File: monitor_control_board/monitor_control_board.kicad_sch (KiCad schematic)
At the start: 21 parts, among them J2 Conn_01x08_Male, J3 Conn_01x08_Male, J5 Conn_01x05_Male, J6 Conn_01x05_Male, SW1 SW_Push, SW2 SW_Push, SW3 SW_Push, SW4 SW_Push, SW5 SW_Push, SW6 SW_Push, U1 TSSP58038

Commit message: osd 컨트롤 보드 좌표 미세 보정
Signed-off-by: Ju, Gyeong-min <jcmh74@gmail.com>
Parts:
- SW1, SW2, SW3, SW4, SW5: footprint Button_Switch_THT:SW_PUSH-12mm -> monitor_control_board_library:SW_PUSH-12mm_Complex
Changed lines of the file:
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@@
     )
     (property "Value" "SW_Push" (id 1) (at 226.695 73.914 0))
-    (property "Footprint" "Button_Switch_THT:SW_PUSH-12mm" (id 2) (at 226.695 67.31 0)
+    (property "Footprint" "monitor_control_board_library:SW_PUSH-12mm_Complex" (id 2) (at 226.695 67.31 0)
       (effects (font (size 1.27 1.27)) hide)
     )
@@
     )
     (property "Value" "SW_Push" (id 1) (at 204.47 73.914 0))
-    (property "Footprint" "Button_Switch_THT:SW_PUSH-12mm" (id 2) (at 204.47 67.31 0)
+    (property "Footprint" "monitor_control_board_library:SW_PUSH-12mm_Complex" (id 2) (at 204.47 67.31 0)
       (effects (font (size 1.27 1.27)) hide)
     )
@@
     )
     (property "Value" "SW_Push" (id 1) (at 203.835 51.054 0))
-    (property "Footprint" "Button_Switch_THT:SW_PUSH-12mm" (id 2) (at 203.835 44.45 0)
+    (property "Footprint" "monitor_control_board_library:SW_PUSH-12mm_Complex" (id 2) (at 203.835 44.45 0)
       (effects (font (size 1.27 1.27)) hide)
     )
@@
   (symbol (lib_id "power:PWR_FLAG") (at 81.28 53.34 270) (unit 1)
     (in_bom yes) (on_board yes) (fields_autoplaced)
-    (property "Reference" "#FLG?" (id 0) (at 83.185 53.34 0)
+    (property "Reference" "#FLG0101" (id 0) (at 83.185 53.34 0)
       (effects (font (size 1.27 1.27)) hide)
     )
@@
     )
     (property "Value" "SW_Push" (id 1) (at 204.47 97.409 0))
-    (property "Footprint" "Button_Switch_THT:SW_PUSH-12mm" (id 2) (at 204.47 90.805 0)
+    (property "Footprint" "monitor_control_board_library:SW_PUSH-12mm_Complex" (id 2) (at 204.47 90.805 0)
       (effects (font (size 1.27 1.27)) hide)
     )
@@
     )
     (property "Value" "SW_Push" (id 1) (at 181.61 74.549 0))
-    (property "Footprint" "Button_Switch_THT:SW_PUSH-12mm" (id 2) (at 181.61 67.945 0)
+    (property "Footprint" "monitor_control_board_library:SW_PUSH-12mm_Complex" (id 2) (at 181.61 67.945 0)
       (effects (font (size 1.27 1.27)) hide)
     )
@@
   (symbol_instances
     (path "/94b5e945-5454-483f-a874-b3e91dafa008"
-      (reference "#FLG?") (unit 1) (value "PWR_FLAG") (footprint "")
+      (reference "#FLG0101") (unit 1) (value "PWR_FLAG") (footprint "")
     )
     (path "/bc319651-4db4-432c-99a9-47f722955312"
@@
     )
     (path "/d0754a39-0cf1-4bbe-83a4-6155f2cbc878"
-      (reference "SW1") (unit 1) (value "SW_Push") (footprint "Button_Switch_THT:SW_PUSH-12mm")
+      (reference "SW1") (unit 1) (value "SW_Push") (footprint "monitor_control_board_library:SW_PUSH-12mm_Complex")
     )
     (path "/4d2bcc63-a2dd-418c-bd5f-ddaef4fca43f"
-      (reference "SW2") (unit 1) (value "SW_Push") (footprint "Button_Switch_THT:SW_PUSH-12mm")
+      (reference "SW2") (unit 1) (value "SW_Push") (footprint "monitor_control_board_library:SW_PUSH-12mm_Complex")
     )
     (path "/19cf3f75-846d-40c4-99e9-986cfa896c10"
-      (reference "SW3") (unit 1) (value "SW_Push") (footprint "Button_Switch_THT:SW_PUSH-12mm")
+      (reference "SW3") (unit 1) (value "SW_Push") (footprint "monitor_control_board_library:SW_PUSH-12mm_Complex")
     )
     (path "/98e08b96-ee1b-4bfe-acf7-0dc72d6a3691"
-      (reference "SW4") (unit 1) (value "SW_Push") (footprint "Button_Switch_THT:SW_PUSH-12mm")
+      (reference "SW4") (unit 1) (value "SW_Push") (footprint "monitor_control_board_library:SW_PUSH-12mm_Complex")
     )
     (path "/1436a783-6564-4cf1-b04a-2e5a11e5eb64"
-      (reference "SW5") (unit 1) (value "SW_Push") (footprint "Button_Switch_THT:SW_PUSH-12mm")
+      (reference "SW5") (unit 1) (value "SW_Push") (footprint "monitor_control_board_library:SW_PUSH-12mm_Complex")
     )
     (path "/06fc7b9c-8a77-4564-ae4b-423182fb3d64"

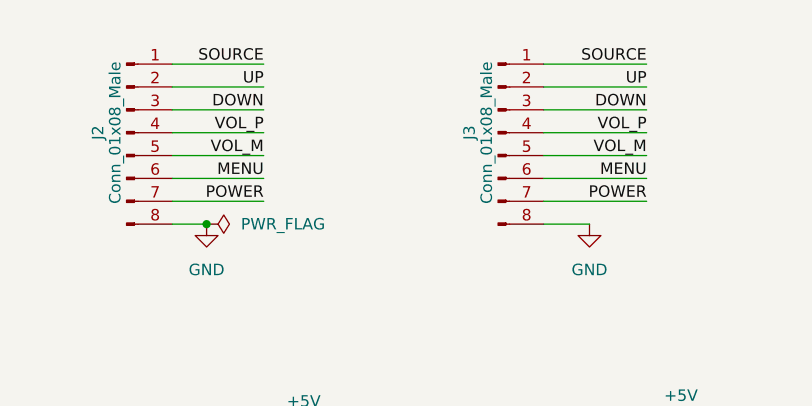
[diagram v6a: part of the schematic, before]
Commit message: osd 컨트롤 보드 GND 핀 추가
Signed-off-by: Ju, Gyeong-min <jcmh74@gmail.com>
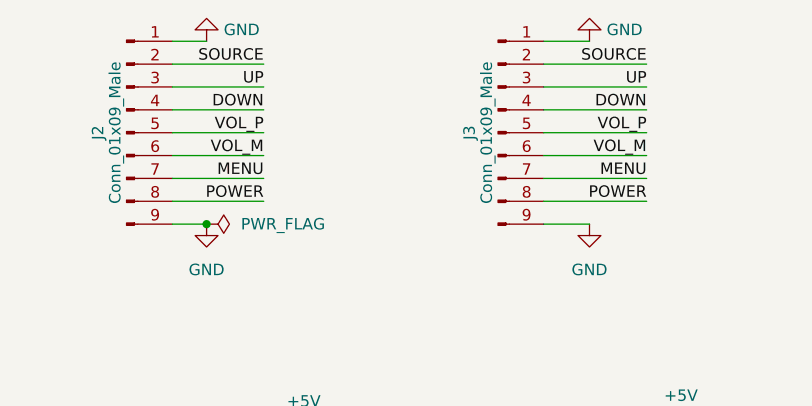
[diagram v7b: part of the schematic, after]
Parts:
- J2: value Conn_01x08_Male -> Conn_01x09_Male; footprint Connector_PinHeader_2.54mm:PinHeader_1x08_P2.54mm_Vertical -> Connector_PinHeader_2.54mm:PinHeader_1x09_P2.54mm_Vertical; symbol Connector:Conn_01x08_Male -> Connector:Conn_01x09_Male
- J3: value Conn_01x08_Male -> Conn_01x09_Male; footprint Connector_JST:JST_PH_S8B-PH-K_1x08_P2.00mm_Horizontal -> Connector_JST:JST_PH_S9B-PH-K_1x09_P2.00mm_Horizontal; symbol Connector:Conn_01x08_Male -> Connector:Conn_01x09_Male
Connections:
- net DOWN: now also J2.4 (Pin_4), J3.4 (Pin_4); no longer J2.3 (Pin_3), J3.3 (Pin_3)
- net GND: now also J2.1 (Pin_1), J2.9 (Pin_9), J3.1 (Pin_1), J3.9 (Pin_9); no longer J2.8 (Pin_8), J3.8 (Pin_8)
- net MENU: now also J2.7 (Pin_7), J3.7 (Pin_7); no longer J2.6 (Pin_6), J3.6 (Pin_6)
- net POWER: now also J2.8 (Pin_8), J3.8 (Pin_8); no longer J2.7 (Pin_7), J3.7 (Pin_7)
- net SOURCE: now also J2.2 (Pin_2), J3.2 (Pin_2); no longer J2.1 (Pin_1), J3.1 (Pin_1)
- net UP: now also J2.3 (Pin_3), J3.3 (Pin_3); no longer J2.2 (Pin_2), J3.2 (Pin_2)
- net VOL_M: now also J2.6 (Pin_6), J3.6 (Pin_6); no longer J2.5 (Pin_5), J3.5 (Pin_5)
- net VOL_P: now also J2.5 (Pin_5), J3.5 (Pin_5); no longer J2.4 (Pin_4), J3.4 (Pin_4)
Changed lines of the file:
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@@
+    (stroke (width 0) (type default) (color 0 0 0 0))
+  )
+  (wire (pts (xy 123.825 33.02) (xy 118.745 33.02))
     (stroke (width 0) (type default) (color 0 0 0 0))
   )
@@
   )
   (wire (pts (xy 87.63 40.64) (xy 77.47 40.64))
+    (stroke (width 0) (type default) (color 0 0 0 0))
+  )
+  (wire (pts (xy 77.47 33.02) (xy 81.28 33.02))
     (stroke (width 0) (type default) (color 0 0 0 0))
   )
@@
     (pin "2")
   )
+  (symbol (lib_id "power:GND") (at 123.825 33.02 180) (unit 1)
+    (in_bom yes) (on_board yes) (fields_autoplaced)
+    (property "Reference" "#PWR0109" (id 0) (at 123.825 26.67 0)
+      (effects (font (size 1.27 1.27)) hide)
+    )
+    (property "Value" "GND" (id 1) (at 125.73 31.7499 0)
+      (effects (font (size 1.27 1.27)) (justify right))
+    )
+    (property "Footprint" "" (id 2) (at 123.825 33.02 0)
+      (effects (font (size 1.27 1.27)) hide)
+    )
+    (property "Datasheet" "" (id 3) (at 123.825 33.02 0)
+      (effects (font (size 1.27 1.27)) hide)
+    )
+    (pin "1")
+  )
   (symbol (lib_id "power:GND") (at 232.41 127.635 0) (unit 1)
     (in_bom yes) (on_board yes)
@@
     (pin "1")
   )
-  (symbol (lib_id "Connector:Conn_01x08_Male") (at 72.39 43.18 0) (unit 1)
+  (symbol (lib_id "Connector:Conn_01x09_Male") (at 72.39 43.18 0) (unit 1)
     (in_bom yes) (on_board yes)
     (property "Reference" "J2" (id 0) (at 69.215 43.18 90))
-    (property "Value" "Conn_01x08_Male" (id 1) (at 71.12 43.18 90))
-    (property "Footprint" "Connector_PinHeader_2.54mm:PinHeader_1x08_P2.54mm_Vertical" (id 2) (at 72.39 43.18 0)
+    (property "Value" "Conn_01x09_Male" (id 1) (at 71.12 43.18 90))
+    (property "Footprint" "Connector_PinHeader_2.54mm:PinHeader_1x09_P2.54mm_Vertical" (id 2) (at 72.39 43.18 0)
       (effects (font (size 1.27 1.27)) hide)
     )
@@
     (pin "7")
     (pin "8")
+    (pin "9")
+  )
+  (symbol (lib_id "power:GND") (at 81.28 33.02 180) (unit 1)
+    (in_bom yes) (on_board yes) (fields_autoplaced)
+    (property "Reference" "#PWR0101" (id 0) (at 81.28 26.67 0)
+      (effects (font (size 1.27 1.27)) hide)
+    )
+    (property "Value" "GND" (id 1) (at 83.185 31.7499 0)
+      (effects (font (size 1.27 1.27)) (justify right))
+    )
+    (property "Footprint" "" (id 2) (at 81.28 33.02 0)
+      (effects (font (size 1.27 1.27)) hide)
+    )
+    (property "Datasheet" "" (id 3) (at 81.28 33.02 0)
+      (effects (font (size 1.27 1.27)) hide)
+    )
+    (pin "1")
   )
   (symbol (lib_id "Connector:TestPoint") (at 189.23 131.445 270) (unit 1)
@@
     (pin "1")
   )
-  (symbol (lib_id "Connector:Conn_01x08_Male") (at 113.665 43.18 0) (unit 1)
+  (symbol (lib_id "Connector:Conn_01x09_Male") (at 113.665 43.18 0) (unit 1)
     (in_bom yes) (on_board yes)
     (property "Reference" "J3" (id 0) (at 110.49 43.18 90))
-    (property "Value" "Conn_01x08_Male" (id 1) (at 112.395 43.18 90))
-    (property "Footprint" "Connector_JST:JST_PH_S8B-PH-K_1x08_P2.00mm_Horizontal" (id 2) (at 113.665 43.18 0)
+    (property "Value" "Conn_01x09_Male" (id 1) (at 112.395 43.18 90))
+    (property "Footprint" "Connector_JST:JST_PH_S9B-PH-K_1x09_P2.00mm_Horizontal" (id 2) (at 113.665 43.18 0)
       (effects (font (size 1.27 1.27)) hide)
     )
@@
     (pin "7")
     (pin "8")
+    (pin "9")
   )
   (symbol (lib_id "Device:C_Polarized_US") (at 120.015 166.37 0) (unit 1)
@@
       (reference "#PWR01") (unit 1) (value "GND") (footprint "")
     )
+    (path "/c2ac00ce-0913-4896-843c-a8ace23112c5"
+      (reference "#PWR0101") (unit 1) (value "GND") (footprint "")
+    )
     (path "/351b09f4-757a-45ed-8f79-a890f5a289e8"
       (reference "#PWR0102") (unit 1) (value "GND") (footprint "")
@@
       (reference "#PWR0108") (unit 1) (value "GND") (footprint "")
     )
+    (path "/6497a330-fbbc-4948-b9f1-fe31c30dcfb1"
+      (reference "#PWR0109") (unit 1) (value "GND") (footprint "")
+    )
     (path "/f4b5f11b-92ad-4b9d-9880-0277b8611810"
       (reference "#PWR0111") (unit 1) (value "GND") (footprint "")
@@
     )
     (path "/bd6046eb-2439-4157-89c1-25727144afe1"
-      (reference "J2") (unit 1) (value "Conn_01x08_Male") (footprint "Connector_PinHeader_2.54mm:PinHeader_1x08_P2.54mm_Vertical")
+      (reference "J2") (unit 1) (value "Conn_01x09_Male") (footprint "Connector_PinHeader_2.54mm:PinHeader_1x09_P2.54mm_Vertical")
     )
     (path "/d3c266d1-a6ac-4741-aed1-d763f0d10aee"
-      (reference "J3") (unit 1) (value "Conn_01x08_Male") (footprint "Connector_JST:JST_PH_S8B-PH-K_1x08_P2.00mm_Horizontal")
+      (reference "J3") (unit 1) (value "Conn_01x09_Male") (footprint "Connector_JST:JST_PH_S9B-PH-K_1x09_P2.00mm_Horizontal")
     )
     (path "/45fa85cf-e83e-46d2-ae9e-e1723a23a31c"

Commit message: 미세 조정
Signed-off-by: Ju, Gyeong-min <jcmh74@gmail.com>
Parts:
- renumbered J3 to J1, J6 to J3, J5 to J4, TP3 to TP1, TP1 to TP2, TP2 to TP3
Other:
- company: (none) -> Amos Home
- title: (none) -> Monitor OSD Control Board
- moved on the sheet: J1, J2, J3, J4, SW1, SW2, SW3, SW4, SW5, SW6, TP1, TP2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
